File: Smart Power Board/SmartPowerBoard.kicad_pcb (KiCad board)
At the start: 4 copper layers, 38.7 x 49.5 mm, 126 parts, among them J1 430450200, J2 USB_C_Receptacle_USB2.0_16P, J3 430450601, J4 Screw_Terminal_01x04, Q1 FDN338P, Q2 FDN338P, Q3 FDN335N, Q4 FDN335N, SW1 SW_Push, SW2 SW_Push, SW3 SW_Push, U1 INA3221, U2 TPS561201DDCR, U4 TPS56C230RJER, U5 TPS56C230RJER, U6 RP2040, U7 W25Q32JVSS, U8 TPS561201DDCR, Y1 FL1200138

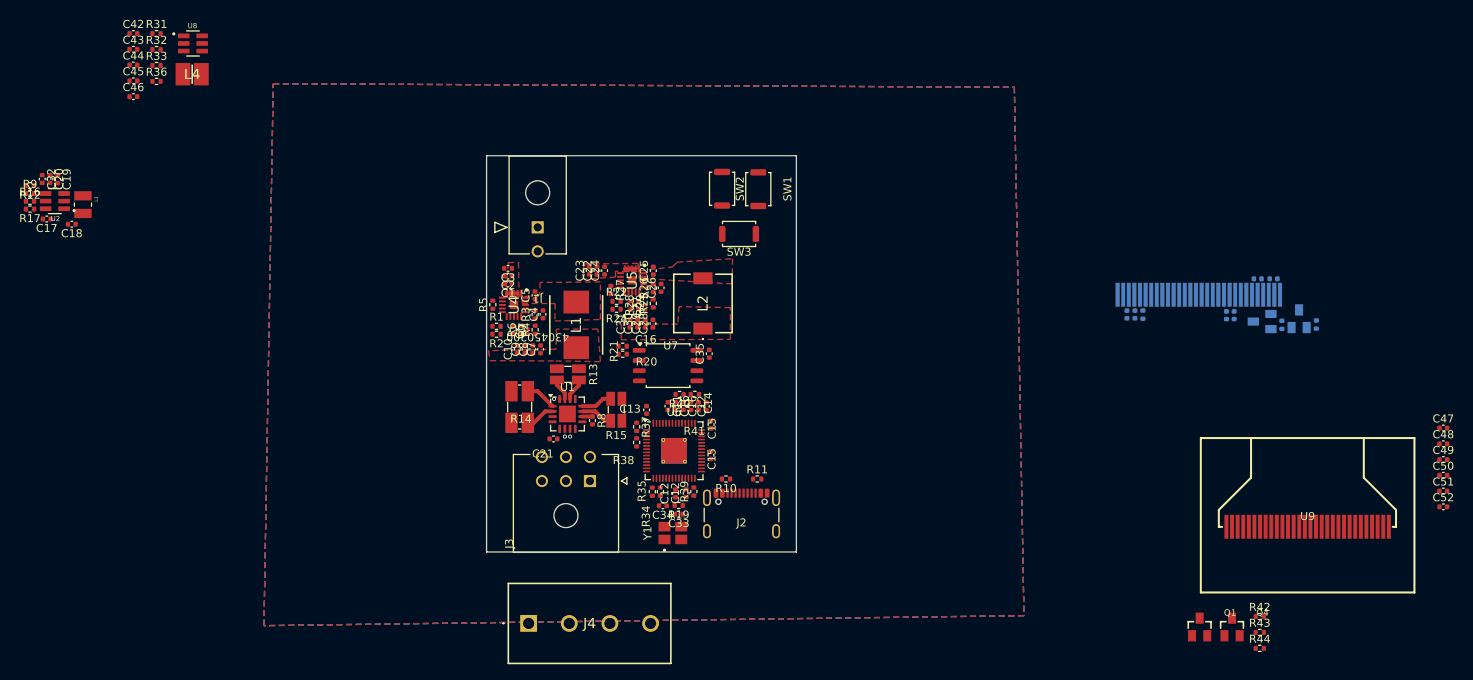
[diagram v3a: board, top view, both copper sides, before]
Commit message: Feat[SmartPowerBoard]: Routing
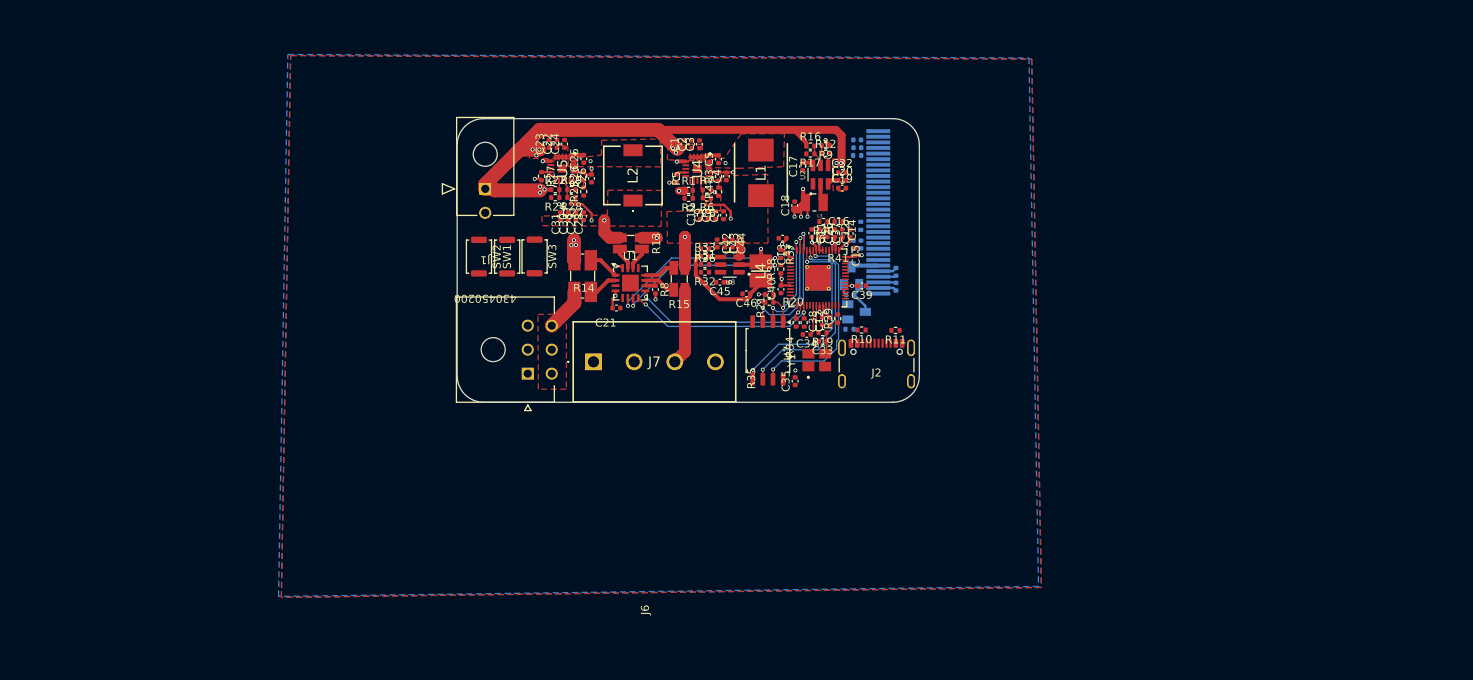
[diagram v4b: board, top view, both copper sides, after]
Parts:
- removed the C12 at (160.9, 118.4)
- removed the C15 at (165.3, 113.6)
- removed the C16 at (160.9, 107.5)
- removed the C16 at (161.9, 107.5)
- removed C41: 1uF, Capacitor_SMD:C_0402_1005Metric
- removed J3: 430450601, 430450601:MOLEX_430450601
- removed J4: Screw_Terminal_01x04, 282857-4_KiCad:2828574
- removed Q2: FDN338P, FDN338P:SSOT-3
- removed Q3: FDN335N, FDN335N:SSOT-3
- removed R23, R30: 47k, Resistor_SMD:R_0402_1005Metric
- removed U3: ~, LIB_X096-2864TMBAG01-H30:X096-2864TMBAG01-H30
- added J6: 430450601, 430450601:MOLEX_430450601, F.Cu at (142.4, 103.4)
- added J7: Screw_Terminal_01x04, 282857-4_KiCad:2828574, F.Cu at (150.6, 101.9)
- C36: value 2.2uF -> 0.1uF; moved to F.Cu
- C37: value 4.7uF -> 0.1uF; moved to F.Cu
- C38, C39, C40: value 1uF -> 0.1uF; moved to F.Cu
- C47, C48, C49, C50, C51, C52, Q1, Q4, R42, R43, R44, U9: moved to B.Cu
- R18: value 620k -> 4.7k
- moved C32 100.0 mm to (181.7, 78.3), turned to 0 degrees
- moved R9 99.6 mm to (179.7, 74.9), turned to 180 degrees
- moved R12 99.6 mm to (179.7, 75.9), turned to 0 degrees
- moved C20 99.0 mm to (181.7, 79.2), turned to 0 degrees
- moved C19 98.1 mm to (181.7, 80.2), turned to 0 degrees
- moved R16 97.8 mm to (177.8, 75.0)
- moved R17 97.8 mm to (177.8, 75.9)
- moved U2 95.8 mm to (179.0, 78.5), turned to 90 degrees
- moved C17 94.7 mm to (176.8, 77.5), turned to 90 degrees
- moved L3 91.4 mm to (178.2, 82.0), turned to 180 degrees
- moved C18 90.4 mm to (175.8, 82.4), turned to 90 degrees
- moved C50 84.4 mm to (183.6, 74.2)
- moved C49 83.0 mm to (183.6, 75.2)
- moved C46 80.5 mm to (169.8, 93.4), turned to 180 degrees
- moved C44 78.1 mm to (168.0, 87.1), turned to -90 degrees
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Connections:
- C26 pad 2: Net-(U5-VCC) -> /Buck Converter 3.3V/V_{CC}
- C36 pad 2: Net-(U3-VCC) -> /MCU/3.3V_{CC}
- C37 pad 2: Net-(U3-VCOMH) -> /MCU/3.3V_{CC}
- C38 pad 1: /MCU/3.3V_{CC} -> GND
- C38 pad 2: GND -> /MCU/3.3V_{CC}
- C39 pad 1: /MCU/3.3V_{CC} -> GND
- C39 pad 2: GND -> /MCU/3.3V_{CC}
- C4 pad 2: Net-(U4-VCC) -> /Buck Converter 5V/V_{CC}
- C40 pad 1: Net-(U3-C2P) -> GND
- C40 pad 2: Net-(U3-C2N) -> /MCU/3.3V_{CC}
- J1 pad 1: GND -> /12V_{IN}
- J1 pad 2: /12V_{IN} -> GND
- L4 pad 1: Net-(U8-SW) -> /Inner Buck Converter 4V/SW
- R13 pad 1: /Triple Channel Monitor/5V_{OUT} -> /Connectors/3.3V_{OUT}
- R13 pad 4: /Buck Converter 5V/5V_{OUT} -> /Buck Converter 3.3V/3.3V_{OUT}
- R14 pad 4: /Triple Channel Monitor/12V_{OUT} -> /Connectors/12V_{OUT}
- R15 pad 1: /Triple Channel Monitor/3.3V_{OUT} -> /Connectors/5V_{OUT}
- R15 pad 4: /Buck Converter 3.3V/3.3V_{OUT} -> /Buck Converter 5V/5V_{OUT}
- R18 pad 1: GND -> /MCU/3.3V_{CC}
- R18 pad 2: Net-(U3-IREF) -> /OLED Display/RES#
- R26 pad 2: Net-(U5-VCC) -> /Buck Converter 3.3V/V_{CC}
- R3 pad 2: Net-(U4-VCC) -> /Buck Converter 5V/V_{CC}
- R39 pad 2: Net-(U6-RUN) -> /MCU/RUN
- SW3 pad 1: GND -> /OLED Display/RES#
- SW3 pad 2: /MCU/RES# -> GND
- U4 pad 17: Net-(U4-VCC) -> /Buck Converter 5V/V_{CC}
- U5 pad 17: Net-(U5-VCC) -> /Buck Converter 3.3V/V_{CC}
- U6 pad 26: Net-(U6-RUN) -> /MCU/RUN
- U6 pad 4: /MCU/EN(3V) -> /Buck Converter 3.3V/EN
- U6 pad 5: /MCU/EN(5V) -> /Buck Converter 5V/EN
- U8 pad 2: Net-(U8-SW) -> /Inner Buck Converter 4V/SW
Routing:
- net /MCU/3.3V_{CC}: track 0.02 -> 110.7 mm, vias 1 -> 18
- net /12V_{IN}: track 2.63 -> 96.7 mm, vias 0 -> 15
- net /MCU/QSPI_SD0: track 0.00 -> 26.1 mm, vias 0 -> 2
- net /MCU/QSPI_SCLK: track 0.00 -> 25.1 mm, vias 0 -> 2
- net /MCU/QSPI_SD3: track 0.00 -> 25.0 mm, vias 0 -> 2
- net /MCU/WARN: track 0.00 -> 24.9 mm, vias 0 -> 2
- net /MCU/CRIT: track 0.00 -> 23.5 mm, vias 0 -> 2
- net /Connectors/3.3V_{OUT}: track 0.00 -> 22.9 mm, vias 0 -> 1
- net /MCU/SCL: track 0.00 -> 22.2 mm, vias 1 -> 2
- net /MCU/SDA: track 0.00 -> 21.0 mm, vias 1 -> 2
- net /MCU/QSPI_SD2: track 0.00 -> 18.5 mm, vias 0 -> 2
- net /MCU/QSPI_SD1: track 0.00 -> 14.9 mm, vias 0 -> 2
- net /Inner Buck Converter 4V/4V_{CC}: track 0.00 -> 14.9 mm
- net /MCU/QSPI_CS: track 0.00 -> 14.2 mm, vias 0 -> 2
- net /Buck Converter 5V/V_{CC}: track 0.00 -> 12.4 mm, vias 0 -> 2
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- added copper zone on F.Cu, net /Connectors/12V_{OUT}
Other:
- board size 38.7 x 49.5 mm -> 57.8 x 35.4 mm

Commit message: Feat[SmartPowerBoard]: More Routing
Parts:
- moved J2 26.6 mm to (188.6, 76.8), turned to 90 degrees
- moved R11 22.9 mm to (183.3, 75.6), turned to 90 degrees
- moved R10 19.3 mm to (183.2, 78.7), turned to -90 degrees
- moved Q4 9.96 mm to (183.6, 105.6)
- moved R18 9.96 mm to (184.1, 94.9)
- moved R43 9.96 mm to (183.7, 86.1)
- moved R44 9.96 mm to (182.7, 107.8)
- moved U9 9.96 mm to (187.1, 93.2)
- moved C47 9.96 mm to (183.2, 97.2)
- moved C48 9.96 mm to (184.1, 97.2)
- moved C49 9.96 mm to (183.7, 85.1)
- moved C50 9.96 mm to (183.7, 84.1)
- moved C51 9.96 mm to (188.5, 102.5)
- moved C52 9.96 mm to (188.5, 100.6)
- moved Q1 9.96 mm to (183.0, 101.1)
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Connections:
- J2 pad A4: /MCU/5V_{IN} -> /Buck Converter 5V/5V_{OUT}
- J2 pad A9: /MCU/5V_{IN} -> /Buck Converter 5V/5V_{OUT}
- J2 pad B4: /MCU/5V_{IN} -> /Buck Converter 5V/5V_{OUT}
- J2 pad B9: /MCU/5V_{IN} -> /Buck Converter 5V/5V_{OUT}
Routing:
- net /OLED Display/RES#: track 0.00 -> 76.3 mm, vias 0 -> 2
- net /MCU/RUN: track 0.00 -> 64.9 mm, vias 0 -> 2
- net /MCU/USB_BOOT: track 0.80 -> 45.6 mm, vias 1 -> 2
- net GND: track 1.25 -> 44.5 mm, vias 1 -> 14
- net /Buck Converter 5V/5V_{OUT}: track 10.6 -> 49.8 mm, vias 3 -> 6
- net /Buck Converter 3.3V/EN: track 2.27 -> 37.5 mm
- net /MCU/3.3V_{CC}: track 110.7 -> 139.6 mm, vias 18 -> 19
- net /Buck Converter 5V/EN: track 2.29 -> 22.1 mm, vias 0 -> 2
- net /MCU/USB_P: track 0.00 -> 12.1 mm, vias 0 -> 2
- net /MCU/USB_M: track 0.00 -> 11.3 mm, vias 0 -> 2
- net Net-(U6-USB_DM): track 0.00 -> 5.59 mm, vias 0 -> 2
- net Net-(U6-USB_DP): track 0.00 -> 5.47 mm, vias 0 -> 2
- net /Connectors/12V_{OUT}: track 5.39 -> 7.69 mm
- net Net-(U9-VCC): track 0.00 -> 2.28 mm
- net /Connectors/5V_{OUT}: track 9.53 -> 11.8 mm
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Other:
- board size 57.8 x 35.4 mm -> 58.8 x 38 mm

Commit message: Feat[SmartPowerBoard]: Routing Complete
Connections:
- Q4 pad 1: /OLED Display/GPIO4 -> /MCU/GPIO15
- R44 pad 1: /OLED Display/GPIO4 -> /MCU/GPIO15
- U6 pad 18: unconnected-(U6-GPIO15-Pad18) -> /MCU/GPIO15
- U6 pad 6: /MCU/GPIO4 -> unconnected-(U6-GPIO4-Pad6)
- U9 pad 18: /OLED Display/SCL -> /MCU/SCL
- U9 pad 19: /OLED Display/SDA -> /MCU/SDA
- U9 pad 20: /OLED Display/SDA -> /MCU/SDA
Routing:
- net GND: track 44.5 -> 85.2 mm, vias 14 -> 32
- net /MCU/GPIO15: track 0.00 -> 31.1 mm, vias 0 -> 1
- net /Inner Buck Converter 4V/4V_{CC}: track 14.9 -> 35.6 mm, vias 0 -> 4
- net /MCU/SDA: track 23.0 -> 43.4 mm, vias 2 -> 5
- net /MCU/SCL: track 24.2 -> 38.3 mm, vias 2 -> 3
- net /MCU/1.1V: track 8.52 -> 18.1 mm
- net /MCU/3.3V_{CC}: track 139.6 -> 146.2 mm, vias 19 -> 20
- net /Buck Converter 5V/5V_{OUT}: track 49.8 -> 54.8 mm, vias 6 -> 8
- net /MCU/XIN: track 3.77 -> 8.81 mm
- net /OLED Display/RES#: track 76.3 -> 79.4 mm
- net /Inner Buck Converter 4V/FB: track 0.00 -> 2.44 mm
- net /Inner Buck Converter 4V/EN: track 0.00 -> 2.43 mm
- net Net-(U8-VBST): track 0.00 -> 1.48 mm
- net /MCU/RUN: track 64.9 -> 66.1 mm, vias 2 -> 4
- net /12V_{IN}: track 96.1 -> 97.3 mm
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- added copper zone on F.Cu, net /Inner Buck Converter 4V/4V_{CC}

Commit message: Feat[SmartPowerBoard]: Silkscreen + Ground
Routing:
- net GND: track 85.2 -> 107.6 mm, vias 32 -> 64
- net /Connectors/5V_{OUT}: vias 0 -> 4
- net /Connectors/3.3V_{OUT}: vias 1 -> 4
- net /Connectors/12V_{OUT}: vias 0 -> 8
- net /12V_{IN}: vias 16 -> 34
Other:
- copper layers 4 -> 13

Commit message: Feat[SmartPowerBoard]: Tapeout
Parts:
- C1, C10, C18, C19, C2, C20, C22, C23, C28, C29, C30, C31, C42, C43, C46, C7, C8, C9: footprint Capacitor_SMD:C_0402_1005Metric -> Capacitor_SMD:C_0603_1608Metric
- C47, C48, C49, C50, C51, C52, Q1, Q4, R18, R42, R43, R44, U9: moved to F.Cu
- moved C10 3.03 mm to (161.0, 84.2)
- moved C7 2.94 mm to (164.0, 84.2)
- moved C9 2.51 mm to (162.5, 84.2)
- moved C19 1.65 mm to (182.0, 81.8)
- moved C44 1.47 mm to (168.9, 86.0)
- moved C31 1.36 mm to (145.2, 84.1)
- moved C20 1.12 mm to (182.0, 80.3)
- moved U9 1.02 mm to (186.1, 93.4)
- moved R18 1.01 mm to (184.1, 93.9), turned to -90 degrees
- moved C3 0.99 mm to (164.9, 74.7)
- moved C2 0.93 mm to (163.7, 74.2)
- moved C43 0.89 mm to (167.8, 86.6)
- moved C30 0.86 mm to (146.7, 84.1)
- moved C23 0.75 mm to (144.6, 74.1)
- moved C51 0.73 mm to (189.1, 103.0)
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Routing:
- net /12V_{IN}: track 97.3 -> 111.2 mm, vias 34 -> 21
- net Net-(Q1-Pad1): track 4.25 -> 13.5 mm, vias 0 -> 2
- net /OLED Display/RES#: track 79.4 -> 83.2 mm
- net /Inner Buck Converter 4V/4V_{CC}: track 35.6 -> 38.9 mm
- net /MCU/GPIO15: track 31.1 -> 33.2 mm, vias 1 -> 2
- net /OLED Display/V_{BAT}: track 3.40 -> 5.10 mm
- net /Buck Converter 3.3V/3.3V_{OUT}: track 7.92 -> 9.32 mm, vias 2 -> 4
- net /MCU/SDA: track 43.4 -> 42.1 mm, vias 5 -> 4
- net /MCU/3.3V_{CC}: track 146.2 -> 145.0 mm
- net /Buck Converter 5V/5V_{OUT}: track 54.8 -> 55.7 mm, vias 8 -> 9
- net /MCU/SCL: track 38.3 -> 39.0 mm, vias 3 -> 4
- net GND: track 107.6 -> 107.4 mm, vias 64 -> 99
- net /Connectors/3.3V_{OUT}: vias 4 -> 5
- net /Connectors/12V_{OUT}: vias 8 -> 14
- net /Buck Converter 5V/SW: vias 2 -> 4
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- added copper zone on B.Cu, net /Connectors/12V_{OUT}
- added copper zone on In1.Cu, net /Connectors/12V_{OUT}
- added copper zone on In2.Cu, net /Connectors/12V_{OUT}
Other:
- board size 58.8 x 38 mm -> 59 x 39.3 mm
